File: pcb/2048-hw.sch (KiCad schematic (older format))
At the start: 82 parts

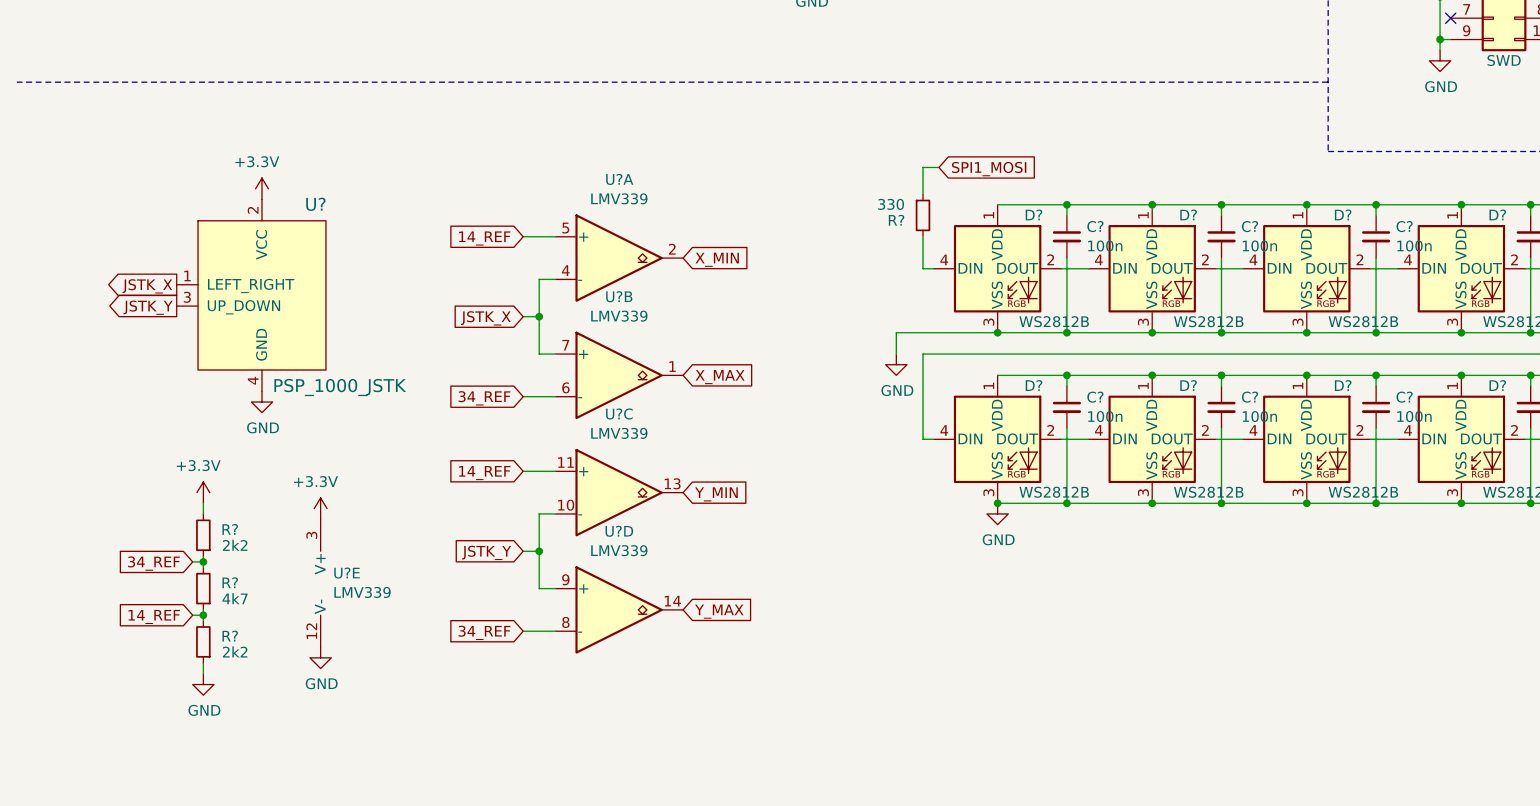
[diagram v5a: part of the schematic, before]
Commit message: Add pushbuttons with debouncers
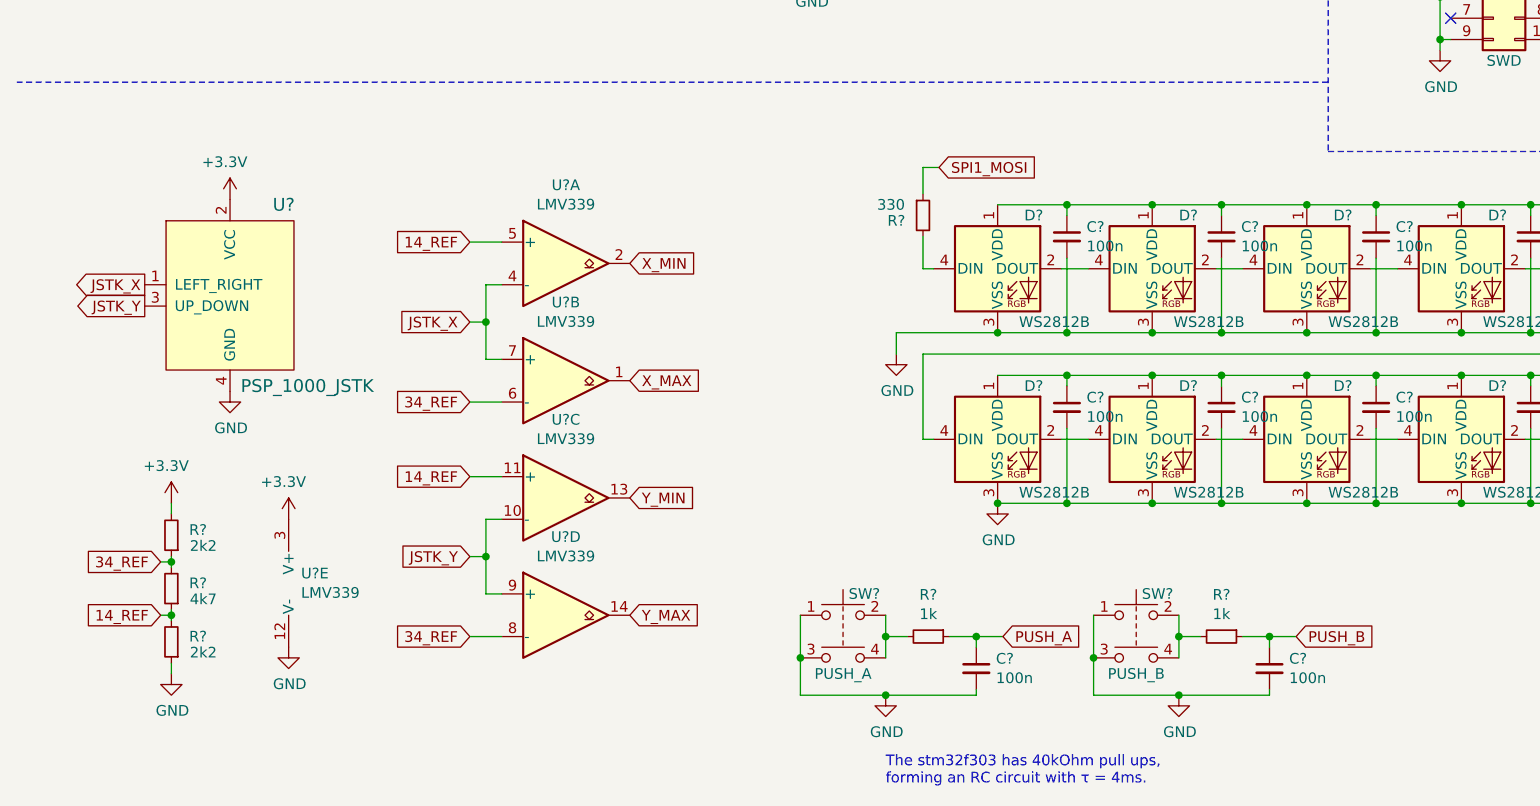
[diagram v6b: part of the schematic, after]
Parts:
- added C? (x2): 100n, symbol Device:C_Small
- added R? (x2): 1k, symbol Device:R_Small
- added SW?: PUSH_A, symbol Switch:SW_Push_Dual
- added SW?: PUSH_B, symbol Switch:SW_Push_Dual
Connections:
- net GND: now also C?.2, C?.2, SW?.1, SW?.1, SW?.3, SW?.3
- new net: R?.2, SW?.2, SW?.4 (x2)
- new net PUSH_A: C?.1, R?.1
- new net PUSH_B: C?.1, R?.1
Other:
- note added: "The stm32f303 has 40kOhm pull ups,\nforming an RC circuit with τ = 4ms."
- moved on the sheet: R?, U?, U?A, U?B, U?C, U?D, U?E

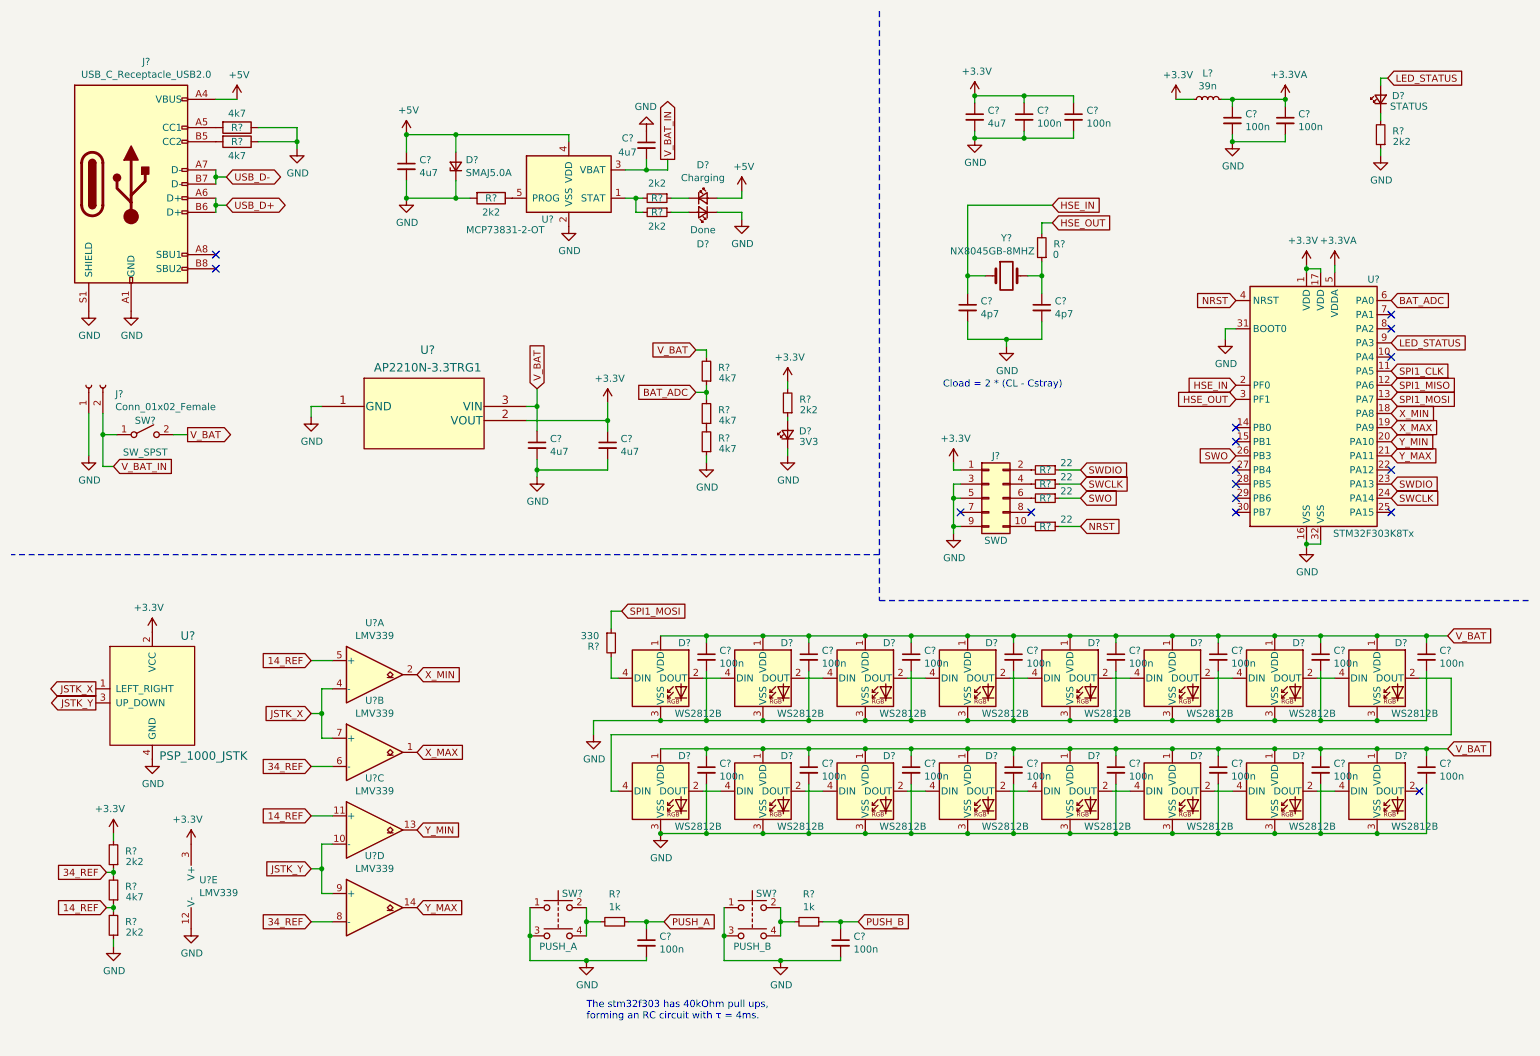
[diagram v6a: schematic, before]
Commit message: Tidy up schematic
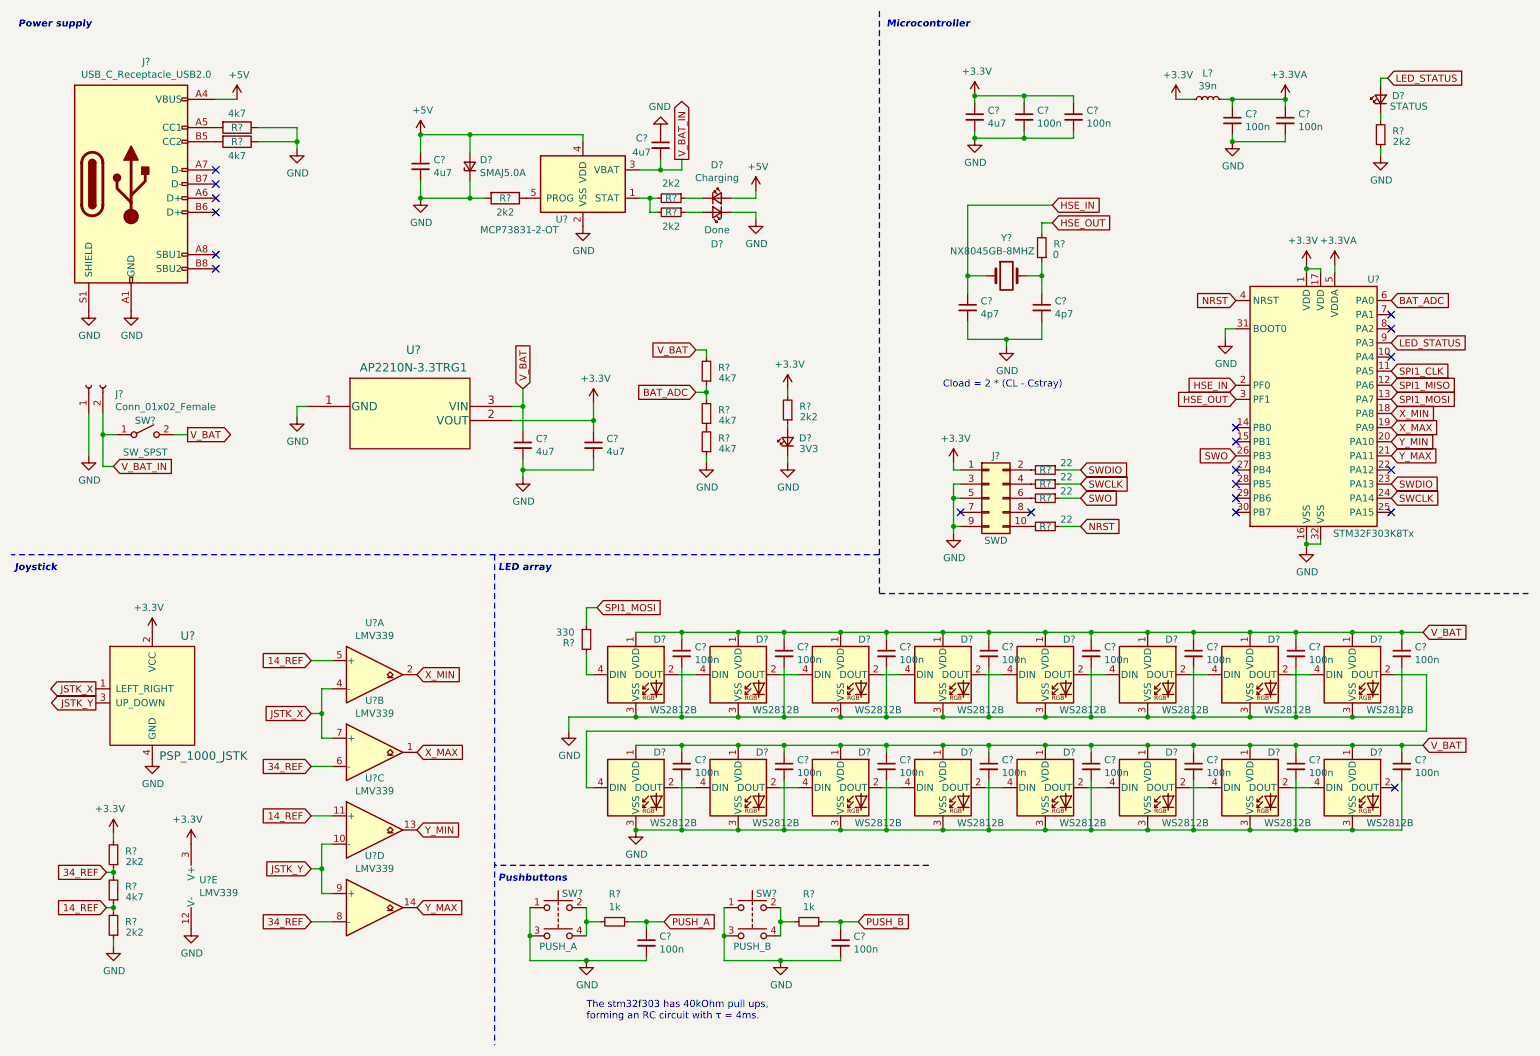
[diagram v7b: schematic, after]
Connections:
- net USB_D+: no longer names the net of J?.A6 (D+)
- net USB_D+: no longer J?.B6 (D+)
- net USB_D-: no longer names the net of J?.A7 (D-)
- net USB_D-: no longer J?.B7 (D-)
- no-connect marks 16 -> 20
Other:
- note added: "Joystick"
- note added: "LED array"
- note added: "Microcontroller"
- note added: "Power supply"
- note added: "Pushbuttons"
- moved on the sheet: C?, D?, R?, U?

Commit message: Add testpoints
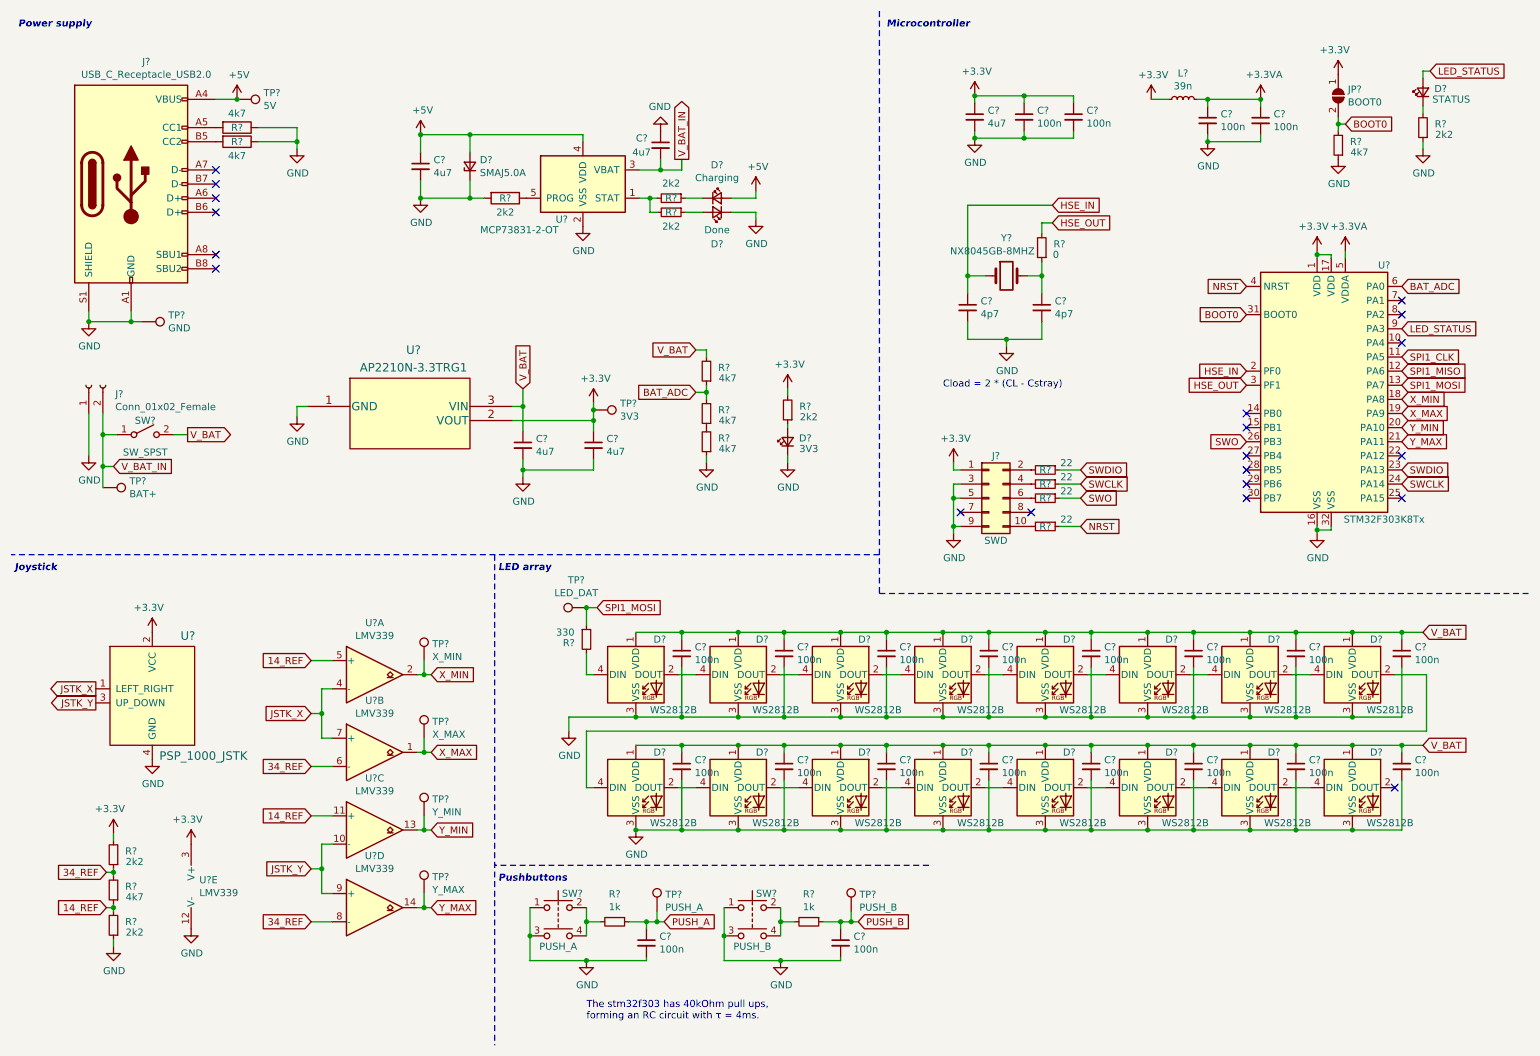
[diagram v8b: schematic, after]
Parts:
- added JP?: BOOT0, symbol Jumper:SolderJumper_2_Open
- added R?: 4k7, symbol Device:R_Small
- added TP?: 5V, symbol Connector:TestPoint
- added TP?: BAT+, symbol Connector:TestPoint
- added TP?: GND, symbol Connector:TestPoint
- added TP?: 3V3, symbol Connector:TestPoint
- added TP?: LED_DAT, symbol Connector:TestPoint
- added TP?: X_MIN, symbol Connector:TestPoint
- added TP?: X_MAX, symbol Connector:TestPoint
- added TP?: Y_MIN, symbol Connector:TestPoint
- added TP?: Y_MAX, symbol Connector:TestPoint
- added TP?: PUSH_A, symbol Connector:TestPoint
- added TP?: PUSH_B, symbol Connector:TestPoint
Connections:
- net +3V3: now also JP?.1 (A), TP?.1
- net +5V: now also TP?.1
- net GND: now also R?.1, TP?.1; no longer U?.31 (BOOT0)
- net PUSH_A: now also TP?.1
- net PUSH_B: now also TP?.1
- net SPI1_MOSI: now also TP?.1
- net V_BAT_IN: now also TP?.1
- net X_MAX: now also TP?.1
- net X_MIN: now also TP?.1
- net Y_MAX: now also TP?.1
- net Y_MIN: now also TP?.1
- new net BOOT0: JP?.2 (B), R?.2, U?.31 (BOOT0)
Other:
- moved on the sheet: C?, D?, L?, R?, U?
